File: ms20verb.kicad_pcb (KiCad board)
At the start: 2 copper layers, 81 x 62.5 mm, 115 parts, among them IC1 BTDR-3, J1 Conn_01x02_Male, J2 Conn_01x02_Male, J3 Conn_01x02_Male, J4 Conn_01x02_Male, J5 Conn_01x04_Male, J6 Conn_01x02_Male, K1 G6S-2, K2 G6S-2, Q1 BC558C, Q2 BC558C, U1 TL074, U2 TL074, U3 LM13700, U4 NE555, U5 NE555, U6 LT1054, U7 L78L05_TO92

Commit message: Resistors to SMD
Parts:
- R1, R10, R11, R12, R13, R14, R15, R16, R17, R18, R19, R2, R20, R21, R22, R23, R24, R25, R26, R27, R28, R29, R3, R30, R31, R32, R33, R34, R35, R36, R37, R38, R39, R4, R40, R5, R6, R7, R8, R9: footprint Resistor_THT:R_Axial_DIN0207_L6.3mm_D2.5mm_P7.62mm_Horizontal -> Resistor_SMD:R_0603_1608Metric; moved to B.Cu
- RV1: renamed from RV3; value A100K -> B100k
- RV2: renamed from RV4; value B10k -> B100K
- RV3: renamed from RV1; value B100k -> A100K
- RV4: renamed from RV2; value B100K -> B10k
- moved D3 274.6 mm to (73.0, 129.1)
- moved U4 249.8 mm to (77.1, 122.8), turned to 90 degrees
- moved TP3 249.4 mm to (61.4, 127.1)
- moved D2 247.1 mm to (61.2, 112.2)
- moved R8 241.4 mm to (82.2, 117.8), turned to 90 degrees
- moved D1 238.4 mm to (61.2, 115.5)
- moved C7 238.4 mm to (88.4, 91.2), turned to 90 degrees
- moved R9 237.3 mm to (79.1, 133.5), turned to 270 degrees
- moved C5 235.1 mm to (110.6, 114.8), turned to 270 degrees
- moved R18 221.2 mm to (91.1, 90.3), turned to 90 degrees
- moved R19 212.2 mm to (110.6, 87.0), turned to 270 degrees
- moved C17 211.1 mm to (88.6, 119.9), turned to 0 degrees
- moved D5 209.0 mm to (127.0, 129.2), turned to 180 degrees
- moved R17 208.9 mm to (103.4, 86.9), turned to 90 degrees
- moved R10 206.8 mm to (117.6, 120.3), turned to 90 degrees
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- renumbered D4 to D1, D6 to D2, D5 to D3, D2 to D4, D3 to D5, D1 to D6, J2 to J1, J1 to J2, J4 to J3, J3 to J4, K2 to K1, K1 to K2, U5 to U4, U4 to U5
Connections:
- D2 pad 2: Net-(D5-Pad2) -> Net-(D2-Pad2)
- D3 pad 1: Net-(D5-Pad1) -> Net-(D3-Pad1)
- D3 pad 2: Net-(D5-Pad2) -> Net-(D2-Pad2)
- D4 pad 2: Net-(D2-Pad2) -> GND
- D5 pad 1: Net-(D3-Pad1) -> Net-(D5-Pad1)
- D5 pad 2: Net-(D2-Pad2) -> Net-(D5-Pad2)
- D6 pad 2: GND -> Net-(D5-Pad2)
- J1 pad 1: Out -> GND
- J1 pad 2: GND -> In
- J2 pad 1: In -> GND
- J2 pad 2: GND -> Out
- J3 pad 1: KillVerbSw1 -> BypassSw1
- J3 pad 2: KillVerbSw2 -> BypassSw2
- J4 pad 1: BypassSw1 -> KillVerbSw1
- J4 pad 2: BypassSw2 -> KillVerbSw2
- K1 pad 10: ReverbOut -> In
- K1 pad 3: FilterOut -> GND
- K1 pad 4: ReverbIn -> EffectIn
- K1 pad 5: GND -> In
- K1 pad 8: FilterOut -> BlendOut
- K1 pad 9: BoostIn -> Out
- K2 pad 10: In -> ReverbOut
- K2 pad 3: GND -> FilterOut
- K2 pad 4: EffectIn -> ReverbIn
- K2 pad 5: In -> GND
- K2 pad 8: BlendOut -> FilterOut
- K2 pad 9: Out -> BoostIn
- RV1 pad 1: FilterOut -> Net-(R15-Pad2)
- RV1 pad 2: Net-(RV3-Pad2) -> Net-(R16-Pad1)
- RV1 pad 3: GND -> Net-(R14-Pad2)
- RV2 pad 1: Net-(IC1-Pad7) -> GND
- RV2 pad 2: Net-(IC1-Pad8) -> Net-(R26-Pad2)
- RV2 pad 3: Net-(IC1-Pad8) -> FreqCV
- RV3 pad 1: Net-(R14-Pad2) -> GND
- RV3 pad 2: Net-(R16-Pad1) -> Net-(RV3-Pad2)
- RV3 pad 3: Net-(R15-Pad2) -> FilterOut
- RV4 pad 1: FreqCV -> Net-(IC1-Pad7)
- RV4 pad 2: Net-(R26-Pad2) -> Net-(IC1-Pad8)
- RV4 pad 3: GND -> Net-(IC1-Pad8)
- U4 pad 2: KillVerbSw1 -> BypassSw1
- U4 pad 3: Net-(D5-Pad2) -> Net-(D2-Pad2)
- U4 pad 6: KillVerbSw1 -> BypassSw1
- U5 pad 2: BypassSw1 -> KillVerbSw1
- U5 pad 3: Net-(D2-Pad2) -> Net-(D5-Pad2)
- U5 pad 6: BypassSw1 -> KillVerbSw1
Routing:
- net +9V: track 48.3 -> 0.00 mm

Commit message: 2 layer dead end
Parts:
- added Q3: J201, Package_TO_SOT_THT:TO-92L_Inline_Wide, F.Cu at (103.7, 114.8)
- added R41: 20k, Resistor_SMD:R_0603_1608Metric, B.Cu at (115.2, 110.9)
- C3, C4: value 5p -> 1p
- R1: value 500k -> 1M
- R3: value 500k -> 200k
- R4, R5, R6, R7: value 100K -> 10k
- moved R15 34.0 mm to (129.9, 83.2)
- moved R23 5.40 mm to (117.3, 99.9)
- moved C3 4.80 mm to (127.5, 105.3), turned to 0 degrees
- moved R35 4.44 mm to (114.7, 99.9)
- moved R34 3.49 mm to (112.2, 99.9)
- moved R30 3.30 mm to (117.4, 81.4)
- moved R17 2.85 mm to (106.2, 86.9)
- moved R27 2.53 mm to (109.6, 99.9)
- moved R10 2.50 mm to (115.1, 120.3)
- moved R5 1.90 mm to (103.7, 86.9), turned to 270 degrees
- moved R19 1.80 mm to (108.8, 87.0)
- moved R25 1.57 mm to (107.1, 99.9)
- moved R36 1.30 mm to (99.4, 99.9)
- moved R7 0.95 mm to (101.2, 86.9)
- moved R16 0.85 mm to (111.3, 87.0)
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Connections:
- C2 pad 2: EffectIn -> Net-(C2-Pad2)
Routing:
- net +9V: track 0.00 -> 223.3 mm, vias 0 -> 3
- net +5V: track 0.00 -> 176.6 mm, vias 0 -> 11
- net Out: track 0.00 -> 167.0 mm
- net FilterOut: track 0.00 -> 144.7 mm, vias 0 -> 2
- net Net-(C6-Pad2): track 0.00 -> 98.0 mm, vias 0 -> 5
- net -9V: track 0.00 -> 79.4 mm, vias 0 -> 4
- net Net-(C2-Pad1): track 0.00 -> 79.0 mm, vias 0 -> 8
- net BlendOut: track 0.00 -> 73.9 mm, vias 0 -> 8
- net Net-(R35-Pad2): track 0.00 -> 70.9 mm, vias 0 -> 5
- net Net-(RV3-Pad2): track 0.00 -> 67.6 mm, vias 0 -> 4
- net ReverbOut: track 0.00 -> 67.4 mm, vias 0 -> 8
- net Net-(D10-Pad2): track 0.00 -> 61.7 mm, vias 0 -> 4
- net Net-(C11-Pad1): track 0.00 -> 60.0 mm, vias 0 -> 6
- net In: track 0.00 -> 59.7 mm
- net FreqCV: track 0.00 -> 58.4 mm, vias 0 -> 4
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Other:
- net class Default: trace_width 0.25 -> 0.3; via_dia 0.8 -> 0.7
- net class Power: trace_width 1 -> 0.6; via_dia 1 -> 0.7; via_drill 0.6 -> 0.4

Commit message: 4-layer board finished
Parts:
- moved D9 44.7 mm to (117.4, 76.3)
- moved D10 43.4 mm to (134.8, 84.6)
- moved R32 42.6 mm to (128.3, 84.5), turned to 270 degrees
- moved TP5 36.7 mm to (88.3, 94.1)
- moved R41 21.0 mm to (100.6, 95.8), turned to 180 degrees
- moved R26 20.5 mm to (100.6, 93.9), turned to 180 degrees
- moved Q3 20.3 mm to (115.0, 97.9)
- moved R21 18.4 mm to (95.7, 80.8)
- moved R39 15.3 mm to (134.2, 99.0), turned to 270 degrees
- moved R15 10.3 mm to (123.0, 75.5)
- moved Q2 9.31 mm to (105.7, 103.1)
- moved Q1 9.31 mm to (109.6, 98.0)
- moved R28 9.31 mm to (102.1, 98.5)
- moved R29 9.31 mm to (102.1, 102.6), turned to 270 degrees
- moved R33 9.31 mm to (100.3, 102.6)
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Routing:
- net +9V: track 223.3 -> 2.36 mm, vias 3 -> 2
- net -9V: track 79.4 -> 209.8 mm, vias 4 -> 1
- net +5V: track 176.6 -> 135.2 mm, vias 11 -> 5
- net Net-(D10-Pad2): track 61.7 -> 22.4 mm, vias 4 -> 0
- net Net-(R35-Pad2): track 70.9 -> 33.8 mm, vias 5 -> 2
- net Net-(C2-Pad1): track 79.0 -> 42.1 mm, vias 8 -> 3
- net Net-(C6-Pad2): track 98.0 -> 64.1 mm, vias 5 -> 0
- net EffectIn: track 39.3 -> 71.8 mm
- net BypassSw2: track 45.0 -> 73.4 mm, vias 3 -> 2
- net Net-(C11-Pad1): track 60.0 -> 34.3 mm, vias 6 -> 0
- net Net-(R22-Pad1): track 30.3 -> 53.3 mm, vias 4 -> 1
- net Net-(R26-Pad2): track 56.9 -> 36.9 mm, vias 3 -> 0
- net CleanOut: track 56.9 -> 75.4 mm, vias 3 -> 1
- net Net-(IC1-Pad8): track 27.5 -> 43.9 mm, vias 0 -> 1
- net Net-(J5-Pad4): track 20.2 -> 3.97 mm, vias 2 -> 0
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- added copper zone on In2.9V.Cu, net +9V
- added copper zone on In1.Gnd.Cu, net GND
- removed copper zone on F.Cu, net GND
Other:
- copper layers 2 -> 4
- net class GND added: clearance 0.2, trace_width 0.6, via_dia 0.7, via_drill 0.4
- net class Power: clearance 0.35 -> 0.32

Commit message: t
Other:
- board text added: "Blend"
- board text added: "Decay"
- board text added: "Frequency"
- board text added: "Resonance"
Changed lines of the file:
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@@
   (general
     (thickness 1.6)
-    (drawings 8)
+    (drawings 12)
     (tracks 806)
     (zones 0)
@@
     (36 B.SilkS user)
     (37 F.SilkS user)
-    (38 B.Mask user hide)
-    (39 F.Mask user hide)
+    (38 B.Mask user)
+    (39 F.Mask user)
     (40 Dwgs.User user)
     (41 Cmts.User user)
@@
     (at 125.66 108.42)
     (descr "<b>16mm / Right-Angle /  PC Mount / Short Pin</b>\n<p>\nFor bottom-mount potentiometers\n<p>\n<a href=\"http://smallbear-electronics.mybigcommerce.com/alpha-single-gang-16mm-right-angle-pc-mount/\">http://smallbear-electronics.mybigcommerce.com/alpha-single-gang-16mm-right-angle-pc-mount/</a>")
-    (fp_text reference RV4 (at 0 -3.175) (layer B.SilkS)
+    (fp_text reference RV4 (at 0 -3.175) (layer B.SilkS) hide
       (effects (font (size 1.2065 1.2065) (thickness 0.1524)) (justify mirror))
     )
@@
     (fp_line (start -1.524 -1.524) (end 1.524 -1.524) (layer B.SilkS) (width 0.127))
     (fp_line (start -6.604 -1.524) (end -3.556 -1.524) (layer B.SilkS) (width 0.127))
-    (fp_text user 1 (at 6.35 -2.54) (layer B.SilkS)
+    (fp_text user 1 (at 7.24 -0.22) (layer B.SilkS)
       (effects (font (size 0.77216 0.77216) (thickness 0.097536)) (justify mirror))
     )
@@
     (at 74.34 108.42)
     (descr "<b>16mm / Right-Angle /  PC Mount / Short Pin</b>\n<p>\nFor bottom-mount potentiometers\n<p>\n<a href=\"http://smallbear-electronics.mybigcommerce.com/alpha-single-gang-16mm-right-angle-pc-mount/\">http://smallbear-electronics.mybigcommerce.com/alpha-single-gang-16mm-right-angle-pc-mount/</a>")
-    (fp_text reference RV2 (at 0 -3.175) (layer B.SilkS)
+    (fp_text reference RV2 (at 0 -3.175) (layer B.SilkS) hide
       (effects (font (size 1.2065 1.2065) (thickness 0.1524)) (justify mirror))
     )
@@
     (at 125.66 80)
     (descr "<b>16mm / Right-Angle /  PC Mount / Short Pin</b>\n<p>\nFor bottom-mount potentiometers\n<p>\n<a href=\"http://smallbear-electronics.mybigcommerce.com/alpha-single-gang-16mm-right-angle-pc-mount/\">http://smallbear-electronics.mybigcommerce.com/alpha-single-gang-16mm-right-angle-pc-mount/</a>")
-    (fp_text reference RV1 (at 0 -3.175) (layer B.SilkS)
+    (fp_text reference RV1 (at 0 -3.175) (layer B.SilkS) hide
       (effects (font (size 1.2065 1.2065) (thickness 0.1524)) (justify mirror))
     )
@@
     (at 74.34 80)
     (descr "<b>16mm / Right-Angle /  PC Mount / Short Pin</b>\n<p>\nFor bottom-mount potentiometers\n<p>\n<a href=\"http://smallbear-electronics.mybigcommerce.com/alpha-single-gang-16mm-right-angle-pc-mount/\">http://smallbear-electronics.mybigcommerce.com/alpha-single-gang-16mm-right-angle-pc-mount/</a>")
-    (fp_text reference RV3 (at 0 -3.175) (layer B.SilkS)
+    (fp_text reference RV3 (at 0 -3.175) (layer B.SilkS) hide
       (effects (font (size 1.2065 1.2065) (thickness 0.1524)) (justify mirror))
     )
@@
     (fp_line (start -1.524 -1.524) (end 1.524 -1.524) (layer B.SilkS) (width 0.127))
     (fp_line (start -6.604 -1.524) (end -3.556 -1.524) (layer B.SilkS) (width 0.127))
-    (fp_text user 1 (at 6.36 -2.3) (layer B.SilkS)
+    (fp_text user 1 (at 7.16 -0.8) (layer B.SilkS)
       (effects (font (size 0.77216 0.77216) (thickness 0.097536)) (justify mirror))
     )
@@
     (fp_line (start 43.5 0) (end 43.5 -54.5) (layer Dwgs.User) (width 0.127))
   )
+  (gr_text Decay (at 130.3 103.2 90) (layer B.SilkS)
+    (effects (font (size 1.5 1.5) (thickness 0.3)) (justify mirror))
+  )
+  (gr_text Frequency (at 80.3 100.7 90) (layer B.SilkS)
+    (effects (font (size 1.5 1.5) (thickness 0.3)) (justify mirror))
+  )
+  (gr_text Resonance (at 76 74.1) (layer B.SilkS)
+    (effects (font (size 1.5 1.5) (thickness 0.3)) (justify mirror))
+  )
+  (gr_text Blend (at 130 74.2) (layer B.SilkS)
+    (effects (font (size 1.5 1.5) (thickness 0.3)) (justify mirror))
+  )
   (gr_line (start 140.5 73) (end 140.5 76.5) (layer Edge.Cuts) (width 0.05))

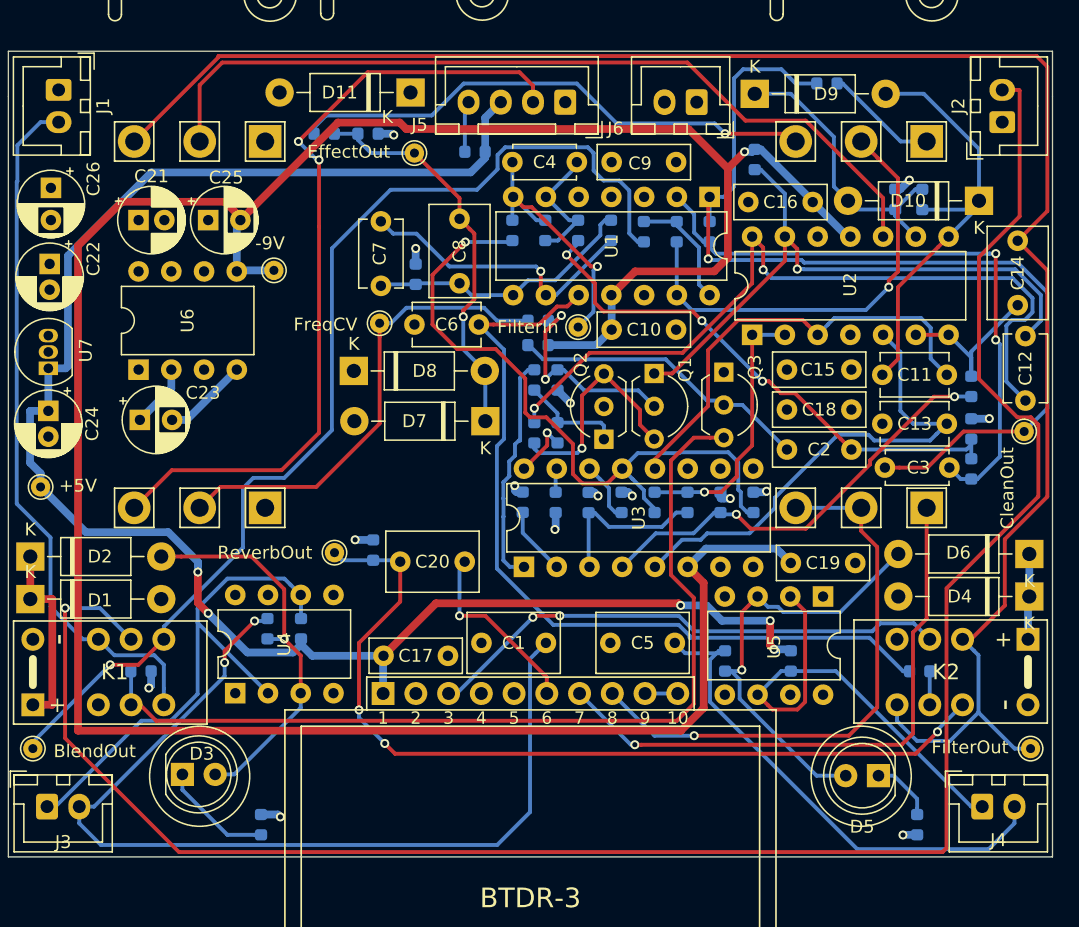
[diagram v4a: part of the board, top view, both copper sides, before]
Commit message: Hand-solder 0603 resistors
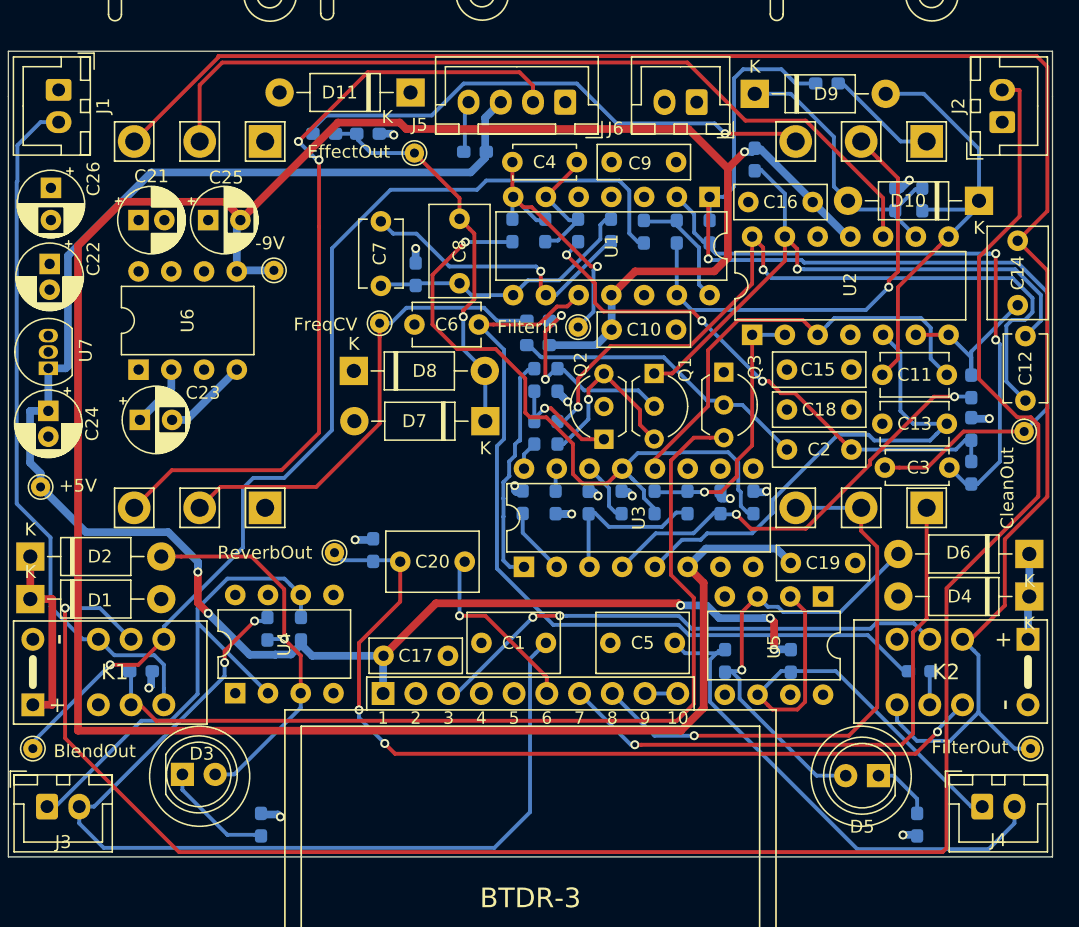
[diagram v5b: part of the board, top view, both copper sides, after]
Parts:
- R1, R10, R11, R12, R13, R14, R15, R16, R17, R18, R19, R2, R20, R21, R22, R23, R24, R25, R26, R27, R28, R29, R3, R30, R31, R32, R33, R34, R35, R36, R37, R38, R39, R4, R40, R41, R5, R6, R7, R8, R9: footprint Resistor_SMD:R_0603_1608Metric -> Resistor_SMD:R_0603_1608Metric_Pad1.05x0.95mm_HandSolder
- moved R29 1.80 mm to (100.3, 102.6)
- moved R33 1.80 mm to (102.1, 102.6)
- moved R4 0.30 mm to (134.2, 105.7)
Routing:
- net Net-(Q1-Pad3): track 17.6 -> 13.9 mm
- net BlendOut: track 85.0 -> 81.4 mm
- net Net-(R29-Pad2): track 4.65 -> 2.24 mm, vias 1 -> 0
- net FilterCtrl: track 8.02 -> 9.30 mm, vias 0 -> 1
- net Net-(C12-Pad2): track 60.4 -> 59.2 mm
- net Net-(C3-Pad2): track 48.5 -> 49.1 mm

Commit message: v1 sent to JLC
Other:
- board text added: "Circuit & Layout by Andrey Salomatin Relay Bypass Switching Circuit by Steve Demedash Base for the MS-20 filter by René Schmitz"
- board text added: "JLCJLCJLCJLC"
- board text added: "П И Н Г v 1"
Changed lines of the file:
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@@
   (general
     (thickness 1.6)
-    (drawings 12)
-    (tracks 809)
+    (drawings 15)
+    (tracks 803)
     (zones 0)
     (modules 117)
@@
   (page A4)
   (layers
-    (0 F.Cu power hide)
-    (1 In1.Gnd.Cu power hide)
-    (2 In2.9V.Cu power hide)
+    (0 F.Cu power)
+    (1 In1.Gnd.Cu power)
+    (2 In2.9V.Cu power)
     (31 B.Cu signal)
-    (32 B.Adhes user hide)
-    (33 F.Adhes user hide)
-    (34 B.Paste user hide)
-    (35 F.Paste user hide)
+    (32 B.Adhes user)
+    (33 F.Adhes user)
+    (34 B.Paste user)
+    (35 F.Paste user)
     (36 B.SilkS user)
-    (37 F.SilkS user hide)
+    (37 F.SilkS user)
     (38 B.Mask user)
     (39 F.Mask user)
@@
     (43 Eco2.User user)
     (44 Edge.Cuts user)
-    (45 Margin user hide)
-    (46 B.CrtYd user)
-    (47 F.CrtYd user)
-    (48 B.Fab user hide)
+    (45 Margin user)
+    (46 B.CrtYd user hide)
+    (47 F.CrtYd user hide)
+    (48 B.Fab user)
     (49 F.Fab user hide)
   )
@@
       (outputformat 1)
       (mirror false)
-      (drillshape 1)
+      (drillshape 0)
       (scaleselection 1)
-      (outputdirectory ""))
+      (outputdirectory "gerbers/"))
   )
   (net 0 "")
@@
     (fp_line (start 43.5 0) (end 43.5 -54.5) (layer Dwgs.User) (width 0.127))
   )
+  (gr_text JLCJLCJLCJLC (at 100 134.3) (layer F.SilkS)
+    (effects (font (size 1 1) (thickness 0.15)))
+  )
+  (gr_text "Circuit & Layout by Andrey Salomatin\nRelay Bypass Switching Circuit by Steve Demedash\nBase for the MS-20 filter by René Schmitz" (at 100 131.9) (layer B.SilkS)
+    (effects (font (size 0.7 0.7) (thickness 0.11)) (justify mirror))
+  )
+  (gr_text "П И Н Г\nv 1" (at 100 127.6) (layer B.Mask)
+    (effects (font (size 1 1) (thickness 0.15)) (justify mirror))
+  )
   (gr_text Decay (at 130.3 103.2 90) (layer B.SilkS)
     (effects (font (size 1.5 1.5) (thickness 0.3)) (justify mirror))
@@
   (segment (start 99.4 110.36) (end 102.04 113) (width 0.3) (layer B.Cu) (net 63))
   (segment (start 99.4 108.775) (end 99.4 110.36) (width 0.3) (layer B.Cu) (net 63))
-  (segment (start 98.4 113) (end 99.5 113) (width 0.3) (layer B.Cu) (net 64))
-  (segment (start 97.9 112.5) (end 98.4 113) (width 0.3) (layer B.Cu) (net 64))
-  (segment (start 97.910001 109.096001) (end 97.9 109.106002) (width 0.3) (layer B.Cu) (net 64))
-  (segment (start 97.9 109.106002) (end 97.9 112.5) (width 0.3) (layer B.Cu) (net 64))
-  (segment (start 97.910001 107.703999) (end 97.910001 109.096001) (width 0.3) (layer B.Cu) (net 64))
-  (segment (start 99.1 103.2) (end 98.8 103.5) (width 0.3) (layer B.Cu) (net 64))
-  (segment (start 98.374 105.956002) (end 97.9 106.430002) (width 0.3) (layer B.Cu) (net 64))
-  (segment (start 99.2 98.3375) (end 99.2 103.2) (width 0.3) (layer B.Cu) (net 64))
-  (segment (start 99.2 103.2) (end 99.1 103.2) (width 0.3) (layer B.Cu) (net 64))
-  (segment (start 98.349999 105.932001) (end 98.374 105.956002) (width 0.3) (layer B.Cu) (net 64))
-  (segment (start 97.9 106.430002) (end 97.9 107.693998) (width 0.3) (layer B.Cu) (net 64))
-  (segment (start 98.349999 104.827999) (end 98.349999 105.932001) (width 0.3) (layer B.Cu) (net 64))
-  (segment (start 97.9 107.693998) (end 97.910001 107.703999) (width 0.3) (layer B.Cu) (net 64))
-  (segment (start 98.8 104.377998) (end 98.349999 104.827999) (width 0.3) (layer B.Cu) (net 64))
-  (segment (start 98.8 103.5) (end 98.8 104.377998) (width 0.3) (layer B.Cu) (net 64))
-  (segment (start 99.825 97.7125) (end 99.2 98.3375) (width 0.3) (layer B.Cu) (net 64))
-  (segment (start 100.3 97.7125) (end 99.825 97.7125) (width 0.3) (layer B.Cu) (net 64))
+  (segment (start 99.825 97.7125) (end 100.3 97.7125) (width 0.3) (layer B.Cu) (net 64))
+  (segment (start 99.2 103.2) (end 99.2 98.3375) (width 0.3) (layer B.Cu) (net 64))
+  (segment (start 97.9 104.5) (end 99.2 103.2) (width 0.3) (layer B.Cu) (net 64))
+  (segment (start 99.2 98.3375) (end 99.825 97.7125) (width 0.3) (layer B.Cu) (net 64))
+  (segment (start 97.910001 107.703999) (end 97.9 107.693998) (width 0.3) (layer B.Cu) (net 64))
+  (segment (start 99.5 113) (end 98.4 113) (width 0.3) (layer B.Cu) (net 64))
+  (segment (start 97.910001 109.096001) (end 97.910001 107.703999) (width 0.3) (layer B.Cu) (net 64))
+  (segment (start 97.9 107.693998) (end 97.9 104.5) (width 0.3) (layer B.Cu) (net 64))
+  (segment (start 97.9 109.106002) (end 97.910001 109.096001) (width 0.3) (layer B.Cu) (net 64))
+  (segment (start 97.9 112.5) (end 97.9 109.106002) (width 0.3) (layer B.Cu) (net 64))
+  (segment (start 98.4 113) (end 97.9 112.5) (width 0.3) (layer B.Cu) (net 64))
   (segment (start 127.36 84.382398) (end 127.36 86.24863) (width 0.3) (layer F.Cu) (net 65))
   (segment (start 116.679999 78.379999) (end 121.357601 78.379999) (width 0.3) (layer F.Cu) (net 65))
